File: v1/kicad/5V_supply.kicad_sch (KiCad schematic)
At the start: 6 parts, among them U15 LM7805

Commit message: Added a DUT board, changed the output connectors , added test hooks, removed unnecessary switches, added FET support
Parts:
- added TP31: GND, symbol Connector:TestPoint_2Pole
- added TP4: 5V, symbol Connector:TestPoint_2Pole
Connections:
- net 5V: now also TP4.2; no longer C33., C34., R40., U15.3 (VO)
- net GND: now also TP31.1, TP31.2
- new net: C33., C34., R40., TP4.1, U15.3 (VO)
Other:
- moved on the sheet: C32, C33, C34, D18, R40, U15

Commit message: Adding KiKit multiboarding
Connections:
- net GND renamed GNDD

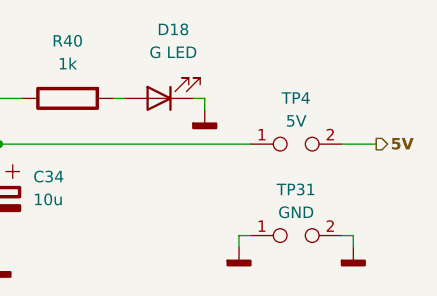
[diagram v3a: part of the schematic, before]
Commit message: Fixed mistakes and made making a BOM easier
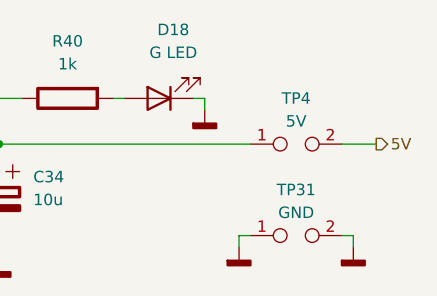
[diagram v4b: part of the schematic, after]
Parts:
- C34: Spend (none) -> $$$
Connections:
- net +15V: now also C32.1; no longer C32.
- net GNDD: now also C32.2, C33.2, C34.2; no longer C32., C33., C34.
- net at D18.2 (A): now also R40.1; no longer R40.
- new net: C33.1, C34.1, R40.2, TP4.1, U15.3 (VO)
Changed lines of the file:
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@@
 			(font
 				(size 1.27 1.27)
-				(thickness 0.254)
-				(bold yes)
+				(thickness 0.1588)
 			)
 			(justify left)
@@
 	)
 	(symbol
-		(lib_name "C_Basic_1")
 		(lib_id "custom:C_Basic")
 		(at 82.55 66.04 0)
@@
 			)
 		)
-		(pin ""
-		)
-		(pin ""
+		(pin "2"
+		)
+		(pin "1"
 		)
 		(instances
@@
 			)
 		)
-		(property "Description" "2-polar test point"
+		(property "Description" ""
 			(at 128.27 69.85 0)
 			(hide yes)
@@
 			)
 		)
-		(property "Description" "2-polar test point"
+		(property "Description" ""
 			(at 128.27 59.69 0)
 			(hide yes)
@@
 			)
 		)
-		(pin ""
-		)
-		(pin ""
+		(pin "1"
+		)
+		(pin "2"
 		)
 		(instances
@@
 	)
 	(symbol
-		(lib_name "R_Basic_2")
 		(lib_id "custom:R_Basic")
 		(at 102.87 54.61 180)
@@
 			)
 		)
-		(pin ""
-		)
-		(pin ""
+		(pin "2"
+		)
+		(pin "1"
 		)
 		(instances
@@
 			)
 		)
-		(pin ""
-		)
-		(pin ""
-		)
-		(instances
+		(property "Spend" "$$$"
+			(at 95.25 66.04 0)
+			(hide yes)
+			(show_name no)
+			(do_not_autoplace no)
+			(effects
+				(font
+					(size 1.27 1.27)
+				)
+			)
+		)
+		(pin "1"
+		)
+		(pin "2"
+		)
+		(instances
